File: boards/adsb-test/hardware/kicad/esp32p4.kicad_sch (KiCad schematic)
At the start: 0 parts

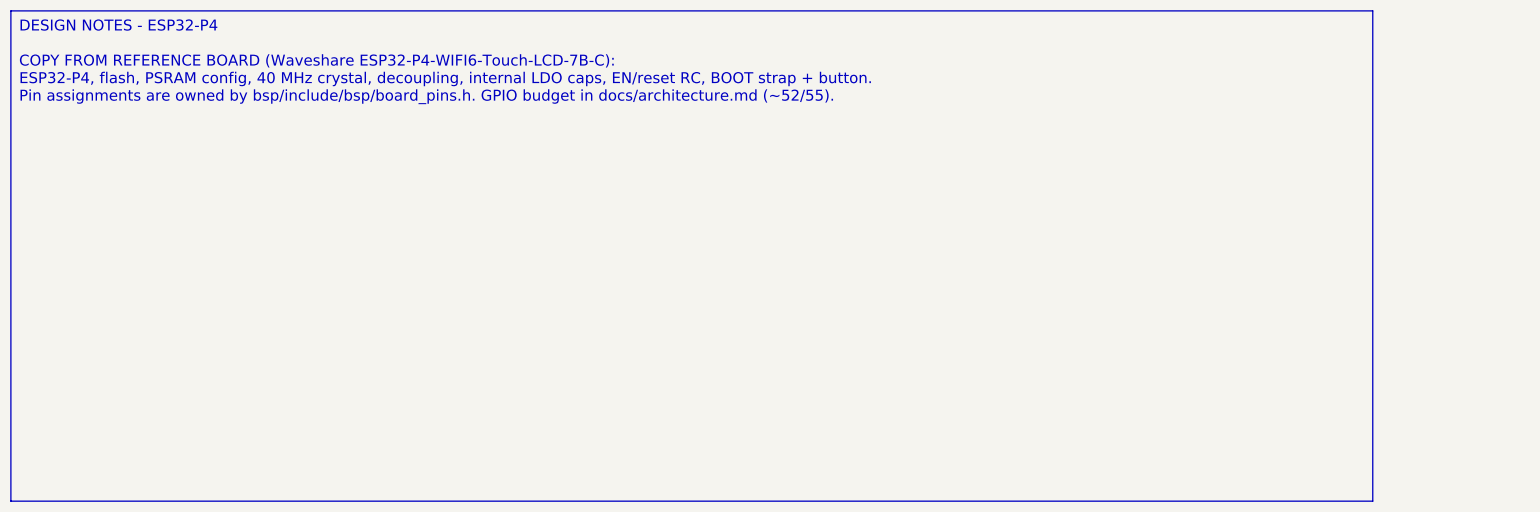
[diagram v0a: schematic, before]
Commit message: Release v0.4.0: ADSB_Test with ESP32-C5, ADSBee m1421 and LA5016 header
- C6 -> C5 co-processor; m1421 identified and integrated (symbol/footprint
  from the ADSBee 1421 carrier, GPL-3.0 attribution)
- Power budget and 2S1P battery sizing for >= 1 h; USB-A for 1-2 SDRs via hub
- Dev port: FT2232H + RP2040 debugprobe; TCA6408A expander for slow I/O
- Test Debug sheet with LA5016 header and rail test points
- Vendor documents git-ignored (public repo)

Co-Authored-By: Claude Opus 5.5 <noreply@anthropic.com>
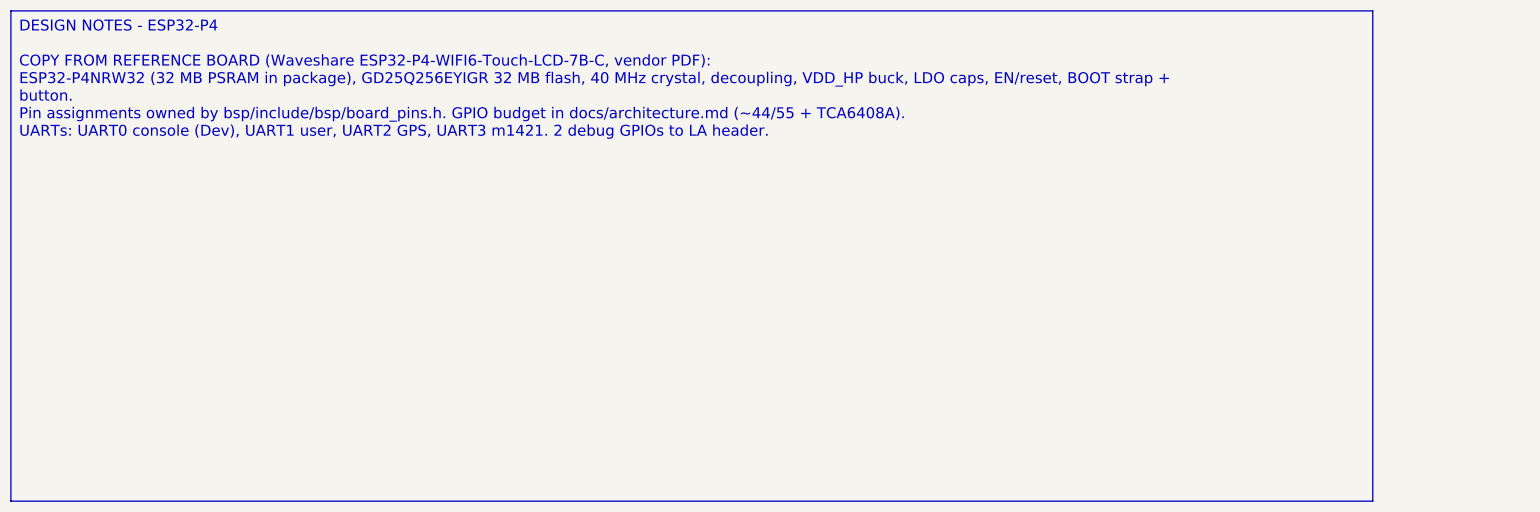
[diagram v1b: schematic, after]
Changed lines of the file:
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@@
 		(comment 1 "Requirements: boards/adsb-test/docs/requirements.md")
 	)
-	(text_box "DESIGN NOTES - ESP32-P4\n\nCOPY FROM REFERENCE BOARD (Waveshare ESP32-P4-WIFI6-Touch-LCD-7B-C):\nESP32-P4, flash, PSRAM config, 40 MHz crystal, decoupling, internal LDO caps, EN/reset RC, BOOT strap + button.\nPin assignments are owned by bsp/include/bsp/board_pins.h. GPIO budget in docs/architecture.md (~52/55)."
+	(text_box "DESIGN NOTES - ESP32-P4\n\nCOPY FROM REFERENCE BOARD (Waveshare ESP32-P4-WIFI6-Touch-LCD-7B-C, vendor PDF):\nESP32-P4NRW32 (32 MB PSRAM in package), GD25Q256EYIGR 32 MB flash, 40 MHz crystal, decoupling, VDD_HP buck, LDO caps, EN/reset, BOOT strap + button.\nPin assignments owned by bsp/include/bsp/board_pins.h. GPIO budget in docs/architecture.md (~44/55 + TCA6408A).\nUARTs: UART0 console (Dev), UART1 user, UART2 GPS, UART3 m1421. 2 debug GPIOs to LA header."
 		(exclude_from_sim no)
 		(at 20 20 0)
